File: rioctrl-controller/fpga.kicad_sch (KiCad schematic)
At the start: 41 parts, among them J10 Conn_02x06_Odd_Even, J8 Conn_02x05_PH, Q1 BSS138W, Q2 BSS138W, Q3 BSS138W, U10 W25Q16JVSS, U9 ECP5U_45_CABGA256, X1 OSC_25MHz

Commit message: Ditch the separate backplane board, increase the slot bitwidth to 12
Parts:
- added TP10, TP11, TP13: TP_1MM, TestPoint:TestPoint_Pad_D1.0mm, symbol hadv-mechanical:TP_1MM
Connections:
- net SlotEN is gone; now on net SA1: U9.T14 (PR62D/-/RDQ65)
- net MCLK: now also TP13.1
- net SA0: now also U9.T13 (PR65B/-/HS/RDQSN65); no longer U9.A4 (PT6B/-)
- net SA1: no longer U9.B4 (PT11B/-)
- net SA2: now also U9.T15 (PR59D/-/RDQ65); no longer U9.C4 (PT11A/+)
- net SA3: now also U9.P13 (PR62A/+/HS/RDQ65); no longer U9.D4 (PT9B/-)
- net SA4: now also U9.R16 (PR44B/-/VREF1_3/HS/RDQ41); no longer U9.E4 (PT9A/+)
- net SA5: now also U9.P15 (PR41B/-/HS/RDQSN41); no longer U9.B5 (PT15B/-)
- net SA6: now also U9.R13 (PR62C/+/RDQ65); no longer U9.C5 (PT15A/+)
- net SA7: now also U9.R14 (PR62B/-/HS/RDQ65); no longer U9.D5 (PT13B/-)
- net SA8: now also U9.R15 (PR59C/+/RDQ65); no longer U9.E5 (PT13A/+)
- net SA9: now also U9.P14 (PR59B/-/HS/RDQ65); no longer U9.A5 (PT18A/+)
- net SB0: now also U9.L16 (PR35A/+/PCLKT3_1/HS/RDQ41); no longer U9.A6 (PT18B/-)
- net SB1: now also U9.K14 (PR29D/-/RDQ29); no longer U9.B6 (PT31B/-)
- net SB2: now also U9.K15 (PR32D/-/PCLKC2_0/RDQ29); no longer U9.C6 (PT31A/+)
- net SB3: now also U9.K16 (PR32C/+/PCLKT2_0/RDQ29); no longer U9.D6 (PT20B/-)
- net SB4: now also U9.J14 (PR29C/+/GR_PCLK2_0/RDQ29); no longer U9.B7 (PT36B/-/PCLKC0_1)
- net SB5: now also U9.J15 (PR32B/-/PCLKC2_1/HS/RDQ29); no longer U9.C7 (PT36A/+/PCLKT0_1)
- net SB6: now also U9.N14 (PR44D/-/RDQ41); no longer U9.D7 (PT33B/-/GR_PCLK0_0)
- net SB7: now also U9.M14 (PR41D/-/RDQ41); no longer U9.A8 (PT38B/-/PCLKC0_0)
- net SB8: now also U9.M15 (PR35D/-/PCLKC3_0/RDQ41); no longer U9.B8 (PT44B/-/PCLKC1_0)
- net SB9: now also U9.M16 (PR35C/+/PCLKT3_0/RDQ41); no longer U9.D8 (PT42B/-/PCLKC1_1)
- net SC0: now also U9.F14 (PR14D/-/RDQ17); no longer U9.A9 (PT51A/+)
- net SC1: now also U9.F15 (PR20C/+/RDQ17); no longer U9.B9 (PT47A/+/GR_PCLK1_0)
- net SC2: now also U9.F16 (PR23A/+/HS/RDQ29); no longer U9.C9 (PT47B/-/GR_PCLK1_1)
- net SC3: now also U9.E14 (PR14C/+/RDQ17); no longer U9.D9 (PT49A/+)
- net SC4: now also U9.E15 (PR17B/-/HS/RDQSN17); no longer U9.A10 (PT51B/-)
- net SC5: now also U9.E16 (PR20D/-/RDQ17); no longer U9.B10 (PT53A/+)
- net SC6: now also U9.H14 (PR23D/-/RDQ29); no longer U9.C10 (PT53B/-)
- net SC7: now also U9.J16 (PR32A/+/PCLKT2_1/HS/RDQ29); no longer U9.D10 (PT56A/+)
- net SC8: now also U9.H15 (PR29B/-/HS/RDQSN29); no longer U9.A11 (PT71A/+)
- net SC9: now also U9.G14 (PR23C/+/VREF1_2/RDQ29); no longer U9.A12 (PT71B/-)
- net SD0: now also U9.D13 (PT80A/+); no longer U9.B11 (PT58A/+)
- net SD1: now also U9.D14 (PR11D/-/RDQ17); no longer U9.C11 (PT58B/-)
- net SD2: now also U9.D16 (PR17A/+/HS/RDQS17); no longer U9.B12 (PT74A/+)
- net SD3: now also U9.C13 (PT78B/-); no longer U9.C12 (PT74B/-)
- net SD4: now also U9.C14 (PR11C/+/RDQ17); no longer U9.A14 (PT83B/-)
- net SD5: now also U9.C16 (PR14A/+/HS/RDQ17); no longer U9.D12 (PT76A/+)
- net SD6: now also U9.C15 (PR14B/-/HS/RDQ17); no longer U9.A13 (PT83A/+)
- net SD7: now also U9.B14 (PT85A/+/URC_GPLL1T_IN); no longer U9.B13 (PT78A/+)
- net SD8: now also U9.B16 (PR11A/+/URC_GPLL0T_IN/HS/RDQ17); no longer U9.C13 (PT78B/-)
- net SD9: now also U9.B15 (PR11B/-/URC_GPLL0C_IN/HS/RDQ17); no longer U9.D13 (PT80A/+)
- net SE0: now also U9.B13 (PT78A/+); no longer U9.B15 (PR11B/-/URC_GPLL0C_IN/HS/RDQ17)
- net SE1: now also U9.A13 (PT83A/+); no longer U9.B16 (PR11A/+/URC_GPLL0T_IN/HS/RDQ17)
- net SE2: now also U9.D12 (PT76A/+); no longer U9.C15 (PR14B/-/HS/RDQ17)
- net SE3: now also U9.C12 (PT74B/-); no longer U9.C16 (PR14A/+/HS/RDQ17)
- net SE4: now also U9.B12 (PT74A/+); no longer U9.D16 (PR17A/+/HS/RDQS17)
- net SE5: now also U9.A12 (PT71B/-); no longer U9.E16 (PR20D/-/RDQ17)
- net SE6: now also U9.D11 (PT69A/+); no longer U9.E15 (PR17B/-/HS/RDQSN17)
- net SE7: now also U9.C11 (PT58B/-); no longer U9.F15 (PR20C/+/RDQ17)
- net SE8: now also U9.B11 (PT58A/+); no longer U9.E14 (PR14C/+/RDQ17)
- net SE9: now also U9.A11 (PT71A/+); no longer U9.F16 (PR23A/+/HS/RDQ29)
- net SF0: now also U9.D9 (PT49A/+); no longer U9.L16 (PR35A/+/PCLKT3_1/HS/RDQ41)
- net SF1: now also U9.C9 (PT47B/-/GR_PCLK1_1); no longer U9.L15 (PR35B/-/PCLKC3_1/HS/RDQ41)
- net SF2: now also U9.B9 (PT47A/+/GR_PCLK1_0); no longer U9.L14 (PR41C/+/RDQ41)
- net SF3: now also U9.A9 (PT51A/+); no longer U9.M16 (PR35C/+/PCLKT3_0/RDQ41)
- net SF4: now also U9.D8 (PT42B/-/PCLKC1_1); no longer U9.M15 (PR35D/-/PCLKC3_0/RDQ41)
- net SF5: now also U9.C8 (PT44A/+/PCLKT1_0); no longer U9.M14 (PR41D/-/RDQ41)
- net SF6: now also U9.B8 (PT44B/-/PCLKC1_0); no longer U9.N16 (PR41A/+/HS/RDQS41)
- net SF7: now also U9.A8 (PT38B/-/PCLKC0_0); no longer U9.P16 (PR44A/+/HS/RDQ41)
- net SF8: now also U9.B6 (PT31B/-); no longer U9.R16 (PR44B/-/VREF1_3/HS/RDQ41)
- net SF9: now also U9.A6 (PT18B/-); no longer U9.T15 (PR59D/-/RDQ65)
- net SPI.CLK: now also U9.P1 (PL44A/+/HS/LDQ41); no longer U9.R2 (PL59C/+/LDQ65)
- net SPI.MISO: now also U9.R2 (PL59C/+/LDQ65); no longer U9.R1 (PL44B/-/VREF1_6/HS/LDQ41)
- net SPI.MOSI: now also U9.R1 (PL44B/-/VREF1_6/HS/LDQ41); no longer U9.P1 (PL44A/+/HS/LDQ41)
- net FPGA_T6: now reaches U9.T6 (PB4A/+/D7/IO7)
- net FPGA_T6: now also TP11.1
- net SD10: now reaches U9.A15 (PT85B/-/URC_GPLL1C_IN)
- net SC10: now reaches U9.G15 (PR23B/-/HS/RDQ29)
- net SC11: now reaches U9.G16 (PR29A/+/GR_PCLK2_1/HS/RDQS29)
- net FPGA_P3: now reaches U9.P3 (PL59B/-/HS/LDQ65)
- net FPGA_P3: now also TP10.1
- new net FPGASlotEN: U9.A4 (PT6B/-)
- new net SA10: U9.P16 (PR44A/+/HS/RDQ41)
- new net SA11: U9.N16 (PR41A/+/HS/RDQS41)
- new net SB10: U9.L14 (PR41C/+/RDQ41)
- new net SB11: U9.L15 (PR35B/-/PCLKC3_1/HS/RDQ41)
- new net SD11: U9.A14 (PT83B/-)
- new net SE10: U9.B10 (PT53A/+)
- new net SE11: U9.A10 (PT51B/-)
- new net SF10: U9.B5 (PT15B/-)
- new net SF11: U9.A5 (PT18A/+)
- no-connect marks 108 -> 96

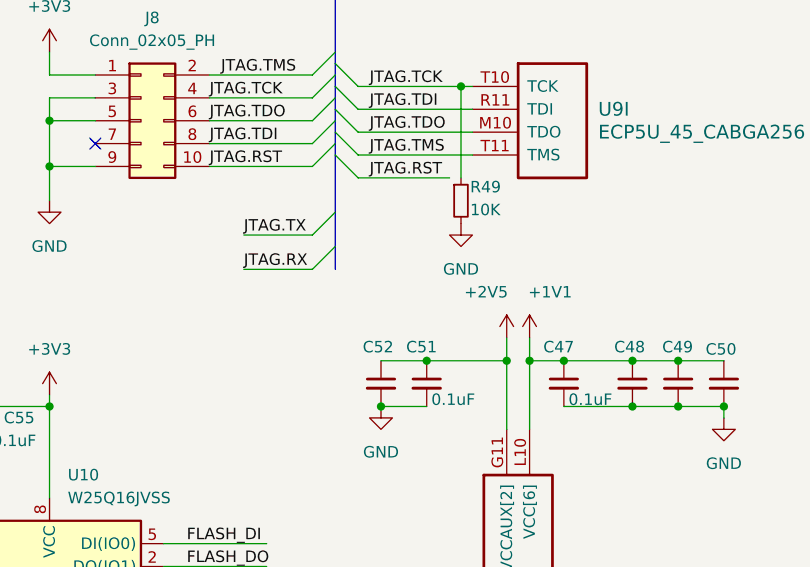
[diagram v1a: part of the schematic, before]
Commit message: Fix ERC, add title information to sch, add initial version of build scripts
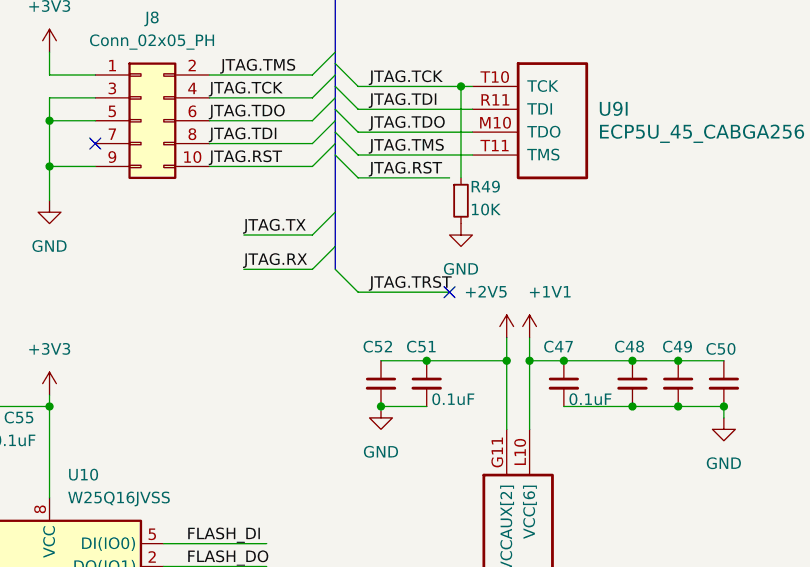
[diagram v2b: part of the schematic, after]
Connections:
- no-connect marks 96 -> 97
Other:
- company: (none) -> R. Veips
- title: (none) -> ${PROJECTNAME}
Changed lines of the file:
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@@
 	(generator_version "8.0")
 	(paper "A3")
+	(title_block
+		(title "${PROJECTNAME}")
+		(date "2024-08-25")
+		(rev "${VERSION}")
+		(company "R. Veips")
+	)
 	(junction
 		(at 293.37 132.08)
@@
 	)
 	(no_connect
+		(at 361.95 52.07)
+	)
+	(no_connect
 		(at 218.44 96.52)
 	)
@@
 	)
 	(bus_entry
+		(at 349.25 49.53)
+		(size 2.54 2.54)
+		(stroke
+			(width 0)
+			(type default)
+		)
+	)
+	(bus_entry
 		(at 349.25 25.4)
 		(size -2.54 2.54)
@@
 	(wire
 		(pts
+			(xy 351.79 52.07) (xy 361.95 52.07)
+		)
+		(stroke
+			(width 0)
+			(type default)
+		)
+	)
+	(wire
+		(pts
 			(xy 210.82 91.44) (xy 218.44 91.44)
 		)
@@
 	(bus
 		(pts
+			(xy 349.25 36.83) (xy 349.25 43.18)
+		)
+		(stroke
+			(width 0)
+			(type default)
+		)
+	)
+	(bus
+		(pts
 			(xy 106.68 116.84) (xy 106.68 119.38)
 		)
@@
 	(bus
 		(pts
-			(xy 349.25 36.83) (xy 349.25 43.18)
-		)
-		(stroke
-			(width 0)
-			(type default)
-		)
-	)
-	(bus
-		(pts
 			(xy 106.68 104.14) (xy 106.68 106.68)
 		)
@@
 		(fields_autoplaced yes)
 		(effects
+			(font
+				(size 1.27 1.27)
+			)
+			(justify left bottom)
+		)
+	)
+	(label "JTAG.TRST"
+		(at 353.06 52.07 0)
+		(fields_autoplaced yes)
+		(effects

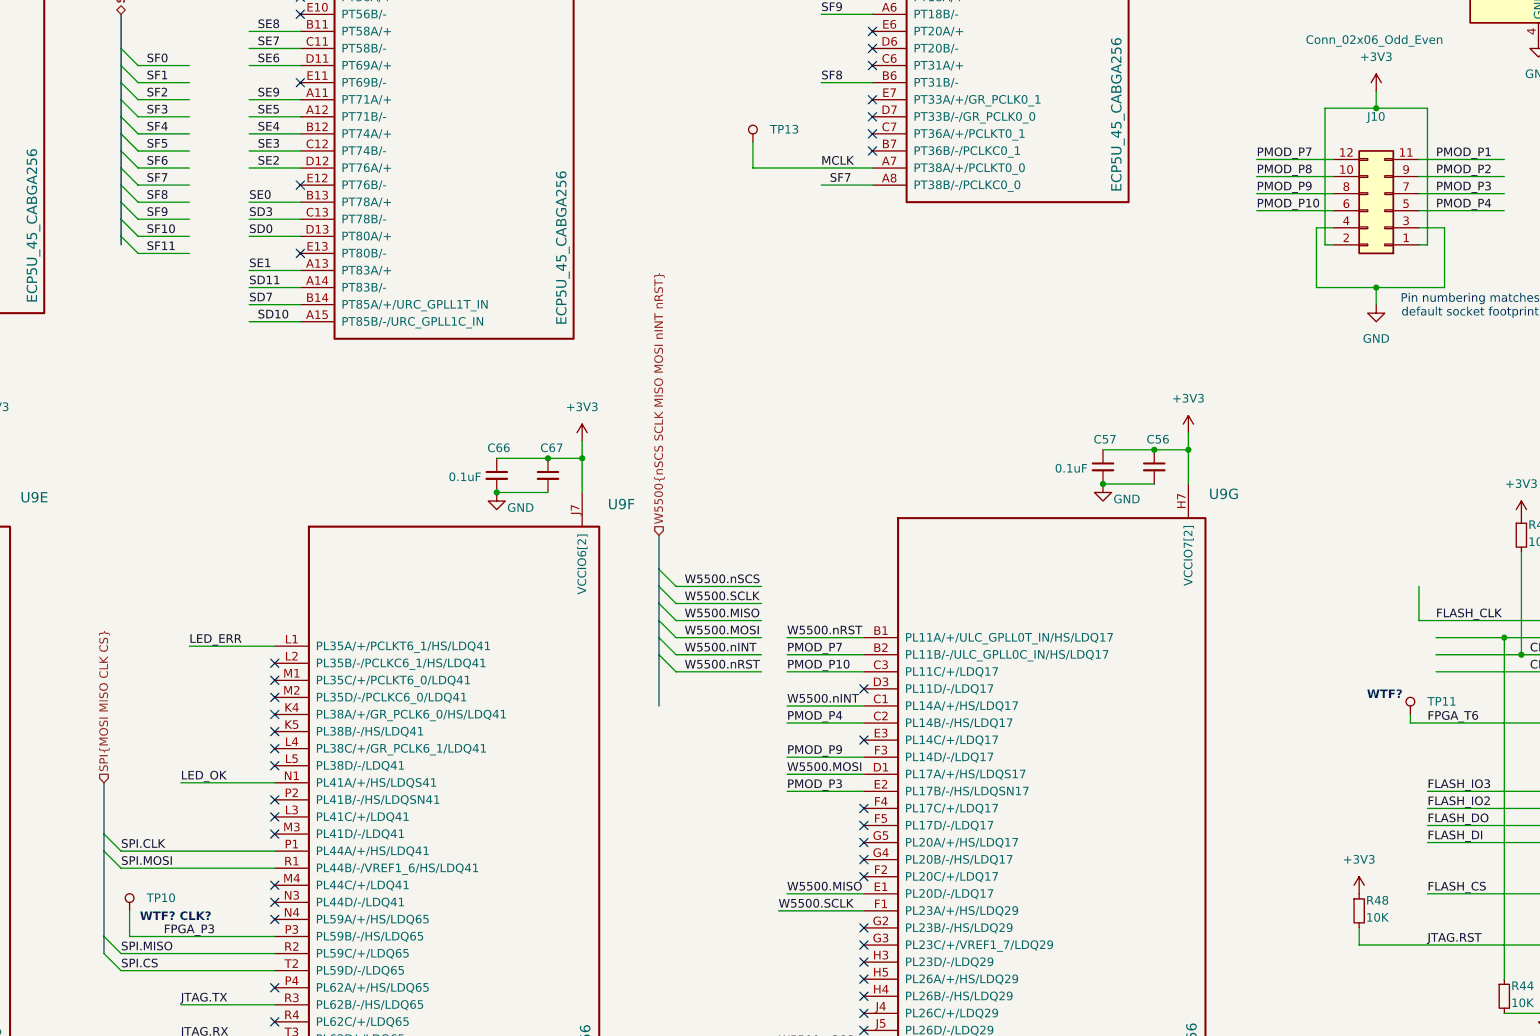
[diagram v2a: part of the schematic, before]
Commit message: Fill in BOM (LCSC#)
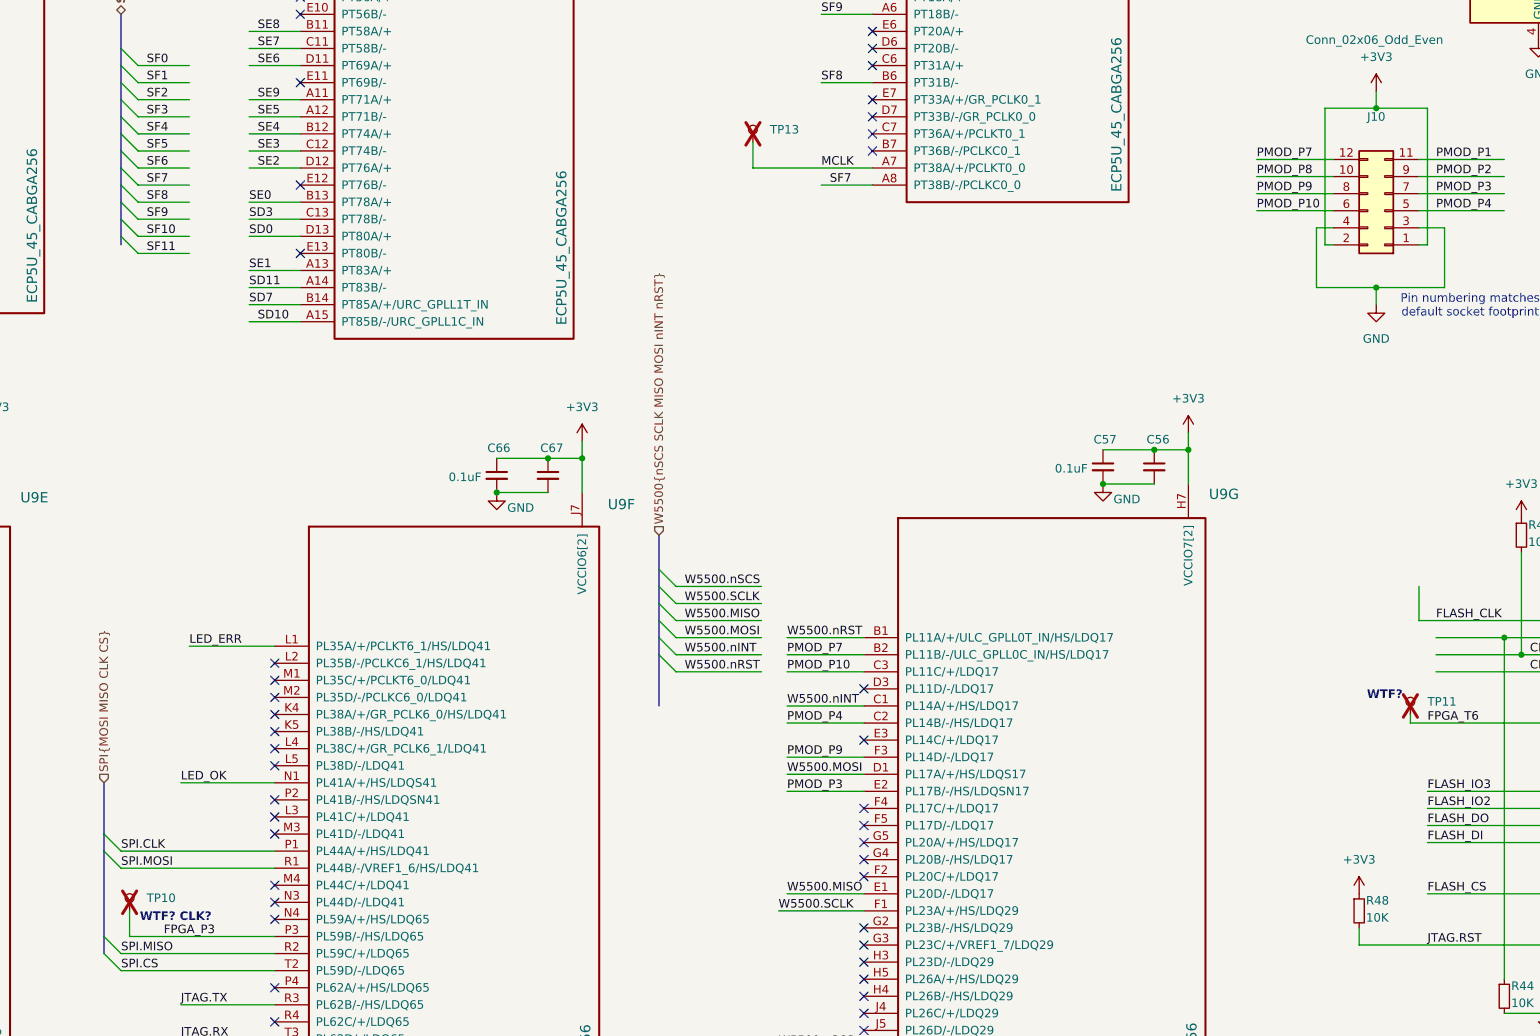
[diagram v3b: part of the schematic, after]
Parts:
- C47, C48, C49, C50, C51, C52, C53, C54, C56, C57, C58, C59, C60, C61, C62, C63, C64, C65, C66, C67: LCSC# (none) -> C56392
- J10: LCSC# (none) -> C2897426
- J8: LCSC# (none) -> C5665
- R44, R45, R46, R48, R49: LCSC# (none) -> C98220
- R50, R51, R52: LCSC# (none) -> C105881
- TP10, TP11, TP13: now not fitted
- U9: LCSC# (none) -> C1550762

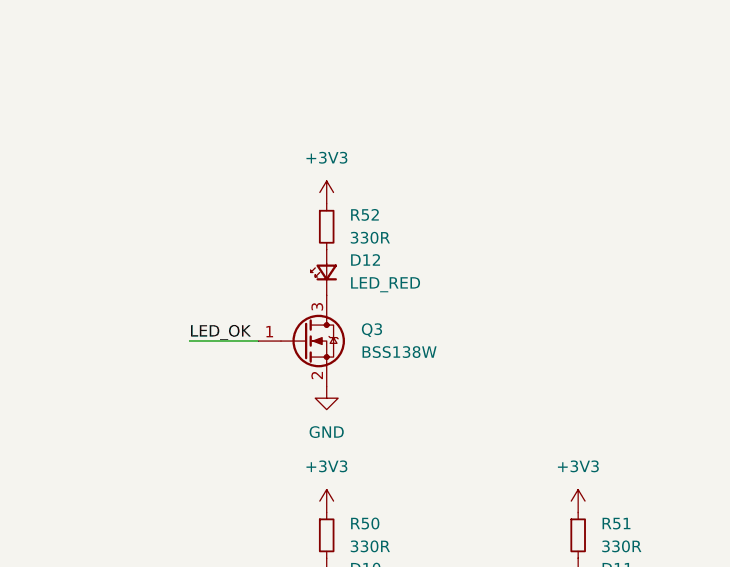
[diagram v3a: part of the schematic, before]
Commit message: Fix minor issues in rioctrl-controller, release v1.1
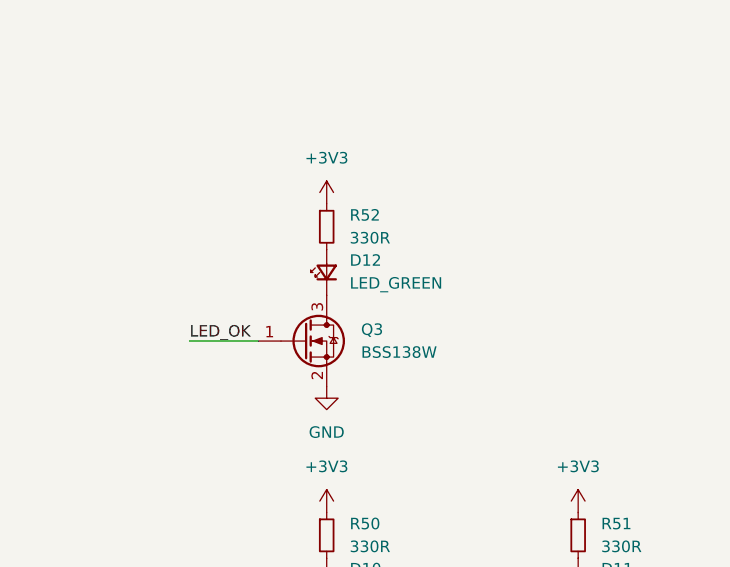
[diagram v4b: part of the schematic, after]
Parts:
- removed D12: LED_RED, LED_SMD:LED_0603_1608Metric, symbol hadv-ui:LED_RED
- added D12: LED_GREEN, LED_SMD:LED_0603_1608Metric, symbol hadv-ui:LED_GREEN
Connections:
- net at R52.2: now also D12.2 (A)
- net at Q3.3 (D): now also D12.1 (K)
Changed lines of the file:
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@@
 	)
 	(symbol
+		(lib_id "hadv-ui:LED_GREEN")
+		(at 439.42 138.43 90)
+		(unit 1)
+		(exclude_from_sim no)
+		(in_bom yes)
+		(on_board yes)
+		(dnp no)
+		(fields_autoplaced yes)
+		(property "Reference" "D12"
+			(at 441.96 137.0964 90)
+			(effects
+				(font
+					(size 1.27 1.27)
+				)
+				(justify right)
+			)
+		)
+		(property "Value" "LED_GREEN"
+			(at 441.96 139.6364 90)
+			(effects
+				(font
+					(size 1.27 1.27)
+				)
+				(justify right)
+			)
+		)
+		(property "Footprint" "LED_SMD:LED_0603_1608Metric"
+			(at 439.42 138.43 90)
+			(effects
+				(font
+					(size 1.27 1.27)
+				)
+				(hide yes)
+			)
+		)
+		(property "Datasheet" "~"
+			(at 439.42 138.43 90)
+			(effects
+				(font
+					(size 1.27 1.27)
+				)
+				(hide yes)
+			)
+		)
+		(property "Description" "LED green"
+			(at 439.42 138.43 0)
+			(effects
+				(font
+					(size 1.27 1.27)
+				)
+				(hide yes)
+			)
+		)
+		(property "MPN" "SZYY0603YG"
+			(at 439.42 138.43 0)
+			(effects
+				(font
+					(size 1.27 1.27)
+				)
+				(hide yes)
+			)
+		)
+		(property "Manufacturer" "Yongyu Photoelectric"
+			(at 439.42 138.43 0)
+			(effects
+				(font
+					(size 1.27 1.27)
+				)
+				(hide yes)
+			)
+		)
+		(property "LCSC#" "C434423"
+			(at 439.42 138.43 0)
+			(effects
+				(font
+					(size 1.27 1.27)
+				)
+				(hide yes)
+			)
+		)
+		(pin "2"
+		)
+		(pin "1"
+		)
+		(instances
+			(project "rioctrl-controller"
+				(path "/41b9ee15-835e-4b63-93e8-ca4d10e95680/0f99be73-1872-4e61-837d-7059db5ce2e1"
+					(reference "D12")
+					(unit 1)
+				)
+			)
+		)
+	)
+	(symbol
 		(lib_id "Device:C_Small")
 		(at 354.33 62.23 0)
@@
 					(unit 1)
 				)
-			)
-		)
-	)
-	(symbol
-		(lib_id "hadv-ui:LED_RED")
-		(at 439.42 138.43 90)
-		(unit 1)
-		(exclude_from_sim no)
-		(in_bom yes)
-		(on_board yes)
-		(dnp no)
-		(fields_autoplaced yes)
-		(property "Reference" "D12"
-			(at 441.96 137.0964 90)
-			(effects
-				(font
-					(size 1.27 1.27)
-				)
-				(justify right)
-			)
-		)
-		(property "Value" "LED_RED"
-			(at 441.96 139.6364 90)
-			(effects
-				(font
-					(size 1.27 1.27)
-				)
-				(justify right)
-			)
-		)
-		(property "Footprint" "LED_SMD:LED_0603_1608Metric"
-			(at 439.42 138.43 90)
-			(effects
-				(font
-					(size 1.27 1.27)
-				)
-				(hide yes)
-			)
-		)
-		(property "Datasheet" "~"
-			(at 439.42 138.43 90)
-			(effects
-				(font
-					(size 1.27 1.27)
-				)
-				(hide yes)
-			)
-		)
-		(property "Description" "LED red"
-			(at 439.42 138.43 0)
-			(effects
-				(font
-					(size 1.27 1.27)
-				)
-				(hide yes)
-			)
-		)
-		(property "MPN" "SZYY0603R"
-			(at 439.42 138.43 0)
-			(effects
-				(font
-					(size 1.27 1.27)
-				)
-				(hide yes)
-			)
-		)
-		(property "Manufacturer" "Yongyu Photoelectric"
-			(at 439.42 138.43 0)
-			(effects
-				(font
-					(size 1.27 1.27)
-				)
-				(hide yes)
-			)
-		)
-		(property "LCSC#" "C434419"
-			(at 439.42 138.43 0)
-			(effects
-				(font
-					(size 1.27 1.27)
-				)
-				(hide yes)
-			)
-		)
-		(pin "1"
-		)
-		(pin "2"
-		)
-		(instances
-			(project "rioctrl-hw"
-				(path "/41b9ee15-835e-4b63-93e8-ca4d10e95680/0f99be73-1872-4e61-837d-7059db5ce2e1"
-					(reference "D12")
-					(unit 1)
-				)
